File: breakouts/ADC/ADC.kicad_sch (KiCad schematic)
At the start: 5 parts, among them U3 ADS1015IDGS

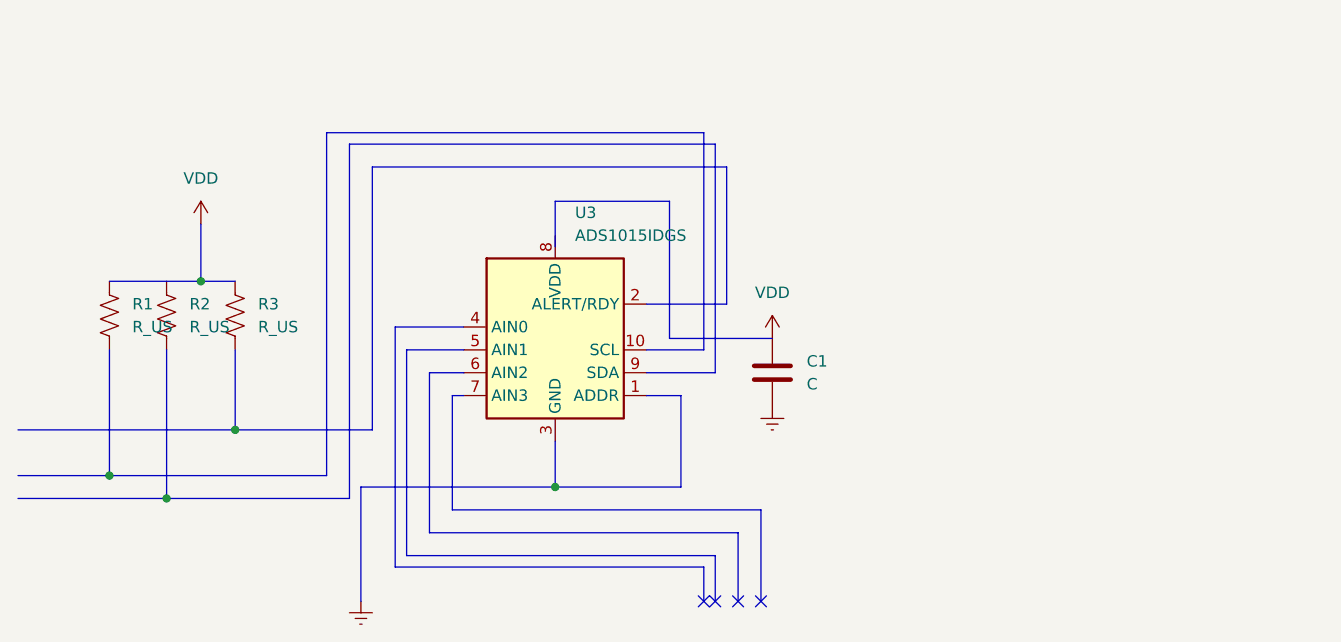
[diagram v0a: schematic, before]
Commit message: Feat[Breakouts}: Bus to wire, organized
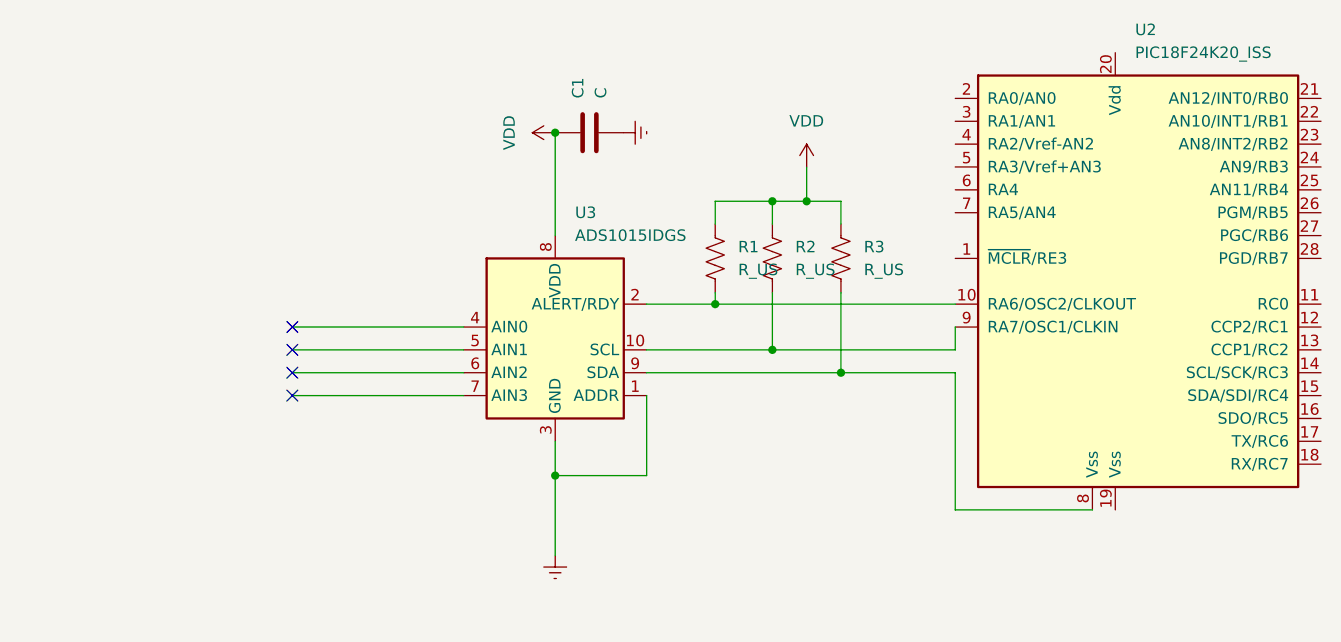
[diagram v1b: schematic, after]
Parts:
- added U2: PIC18F24K20_ISS, Package_SO:SSOP-28_5.3x10.2mm_P0.65mm, symbol MCU_Microchip_PIC18:PIC18F24K20_ISS
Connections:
- net Earth: now also U3.1 (ADDR), U3.3 (GND)
- net VDD: now also R1.1, R2.1, R3.1, U3.8 (VDD)
- net at R1.2: now also U3.2 (ALERT/RDY), U2.10 (RA6/OSC2/CLKOUT)
- net at R3.2: now also U3.9 (SDA), U2.8 (Vss)
- net at R2.2: now also U3.10 (SCL), U2.9 (RA7/OSC1/CLKIN)
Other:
- moved on the sheet: C1, R1, R2, R3

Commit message: Feat[breakouts]: Added TODOs for ADC
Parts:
- added R4: R_Small, symbol Device:R_Small
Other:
- note added: ""earth" ground means that electricity is physically connected to the earth, so that excess surges of electricity can dissipate. In this case we are referring to ground as the common return path for electricity (once your ADC is powered by VDD electricity needs a path to flow back!), so we want to use this symbol."
- note added: "1"
- note added: "1. This is the "earth" ground symbol, which is actually different to the symbol."
- note added: "2"
- note added: "2. Same as 1 - change to the the corrent GND symbol. Also, the GND symbol typically points towards the bottom so u want to rotate this to point to the bottom"
- note added: "3"
- note added: "3. The VDD symbol usually points upwards. You did it for the pull-up resistors so just rotate this upwards"
- note added: "4"
- note added: "4. Rmb this is a breakout board so u don't actually need to slap an MCU on the board. U can just break out the i2c pins (take a look at varit's INA226 breakout board) which can be connected to a pico or arduino or the many other alternatives we alrdy have. But great job thinking above and beyond!"
- note added: "5"
- note added: "5. This is the US symbol for a resistor, we typically use the international resistor symbol. Also, you don't actually need to pull the i2c lines high on a breakout board as it will already be pulled high from the master/central side. So you can remove R2 and R3"
- note added: "6"
- note added: "6. Okay, you've pulled ADDR low, meaning that you will have one i2c address. But what if there are address collisions between peripherals? What if you need to change the address? Read section 8.5 (pages 18-19) of your datasheet and see if you can provide alternative addresses using jumpers (look at varit's INA226 board)"
- note added: "7"
- note added: "7. What's the point of the ADC if it can't take any inputs? You need to break these pins out (probably with a 1x4 2.54mm header pin) so the chip can actually take in an analog input and convert it."
- note added: "Crane, this is some great work you've done. I can see you've put a lot of thought into the schematic and payed a lot of attention to the datasheet. I've left some feedback which you can work on. Also, make sure to reference Byran's ADC in his carrier schematic, and take a look at the other boards in the breakouts folder to get a better sense of what you are doing. Good job!"
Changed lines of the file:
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@@
     (stroke (width 0) (type default))
   )
+  (text "6" (exclude_from_sim no)
+ (at 148.336 93.472 0)
+    (effects (font (size 1.27 1.27)))
+  )
+  (text "1. This is the \"earth\" ground symbol, which is actually different to the     symbol.\n" (exclude_from_sim no)
+    (at 105.156 133.096 0)
+    (effects (font (size 1.27 1.27)))
+  )
+  (text "4. Rmb this is a breakout board so u don't actually need to slap an MCU on the board.\nU can just break out the i2c pins (take a look at varit's INA226 breakout board)\nwhich can be connected to a pico or arduino or the \nmany other alternatives we alrdy have. But great job thinking above and beyond!" (exclude_from_sim no)
+    (at 183.388 113.538 0)
+    (effects (font (size 1.27 1.27)) (justify left))
+  )
+  (text "5. This is the US symbol for a resistor, we typically use the international resistor\nsymbol. Also, you don't actually need to pull the i2c lines high on a breakout board\nas it will already be pulled high from the master/central side. So you can remove R2 and R3" (exclude_from_sim no)
+    (at 174.244 42.926 0)
+    (effects (font (size 1.27 1.27)) (justify left))
+  )
+  (text "7. What's the point of the ADC if it can't take any inputs? You need to break these\npins out (probably with a 1x4 2.54mm header pin) so the chip can actually take in an \nanalog input and convert it." (exclude_from_sim no)
+    (at 16.256 79.502 0)
+    (effects (font (size 1.27 1.27)) (justify left))
+  )
+  (text "2. Same as 1 - change to the the corrent GND symbol. Also, the GND symbol typically points towards\nthe bottom so u want to rotate this to point to the bottom" (exclude_from_sim no)
+    (at 48.514 40.64 0)
+    (effects (font (size 1.27 1.27)) (justify left))
+  )
+  (text "\"earth\" ground means that electricity is physically connected to the\nearth, so that excess surges of electricity can dissipate. In this case we are referring\nto ground as the common return path for electricity (once your ADC is powered by VDD\nelectricity needs a path to flow back!), so we want to use this      symbol." (exclude_from_sim no)
+    (at 62.484 140.208 0)
+    (effects (font (size 1.27 1.27)) (justify left))
+  )
+  (text "5" (exclude_from_sim no)
+ (at 170.688 72.644 0)
+    (effects (font (size 1.27 1.27)))
+  )
+  (text "Crane, this is some great work you've done. I can see you've put a lot of thought\ninto the schematic and payed a lot of attention to the datasheet. I've left some\nfeedback which you can work on. Also, make sure to reference Byran's ADC in his carrier\nschematic, and take a look at the other boards in the breakouts folder to get a better\nsense of what you are doing. Good job!" (exclude_from_sim no)
+    (at 224.536 144.526 0)
+    (effects (font (size 1.27 1.27)))
+  )
+  (text "3" (exclude_from_sim no)
+ (at 134.366 65.278 0)
+    (effects (font (size 1.27 1.27)))
+  )
+  (text "6. Okay, you've pulled ADDR low, meaning that you will have one i2c address. But what if \nthere are address collisions between peripherals? What if you need to change the address?\nRead section 8.5 (pages 18-19) of your datasheet and see if you can provide alternative\naddresses using jumpers (look at varit's INA226 board)" (exclude_from_sim no)
+    (at 19.812 118.872 0)
+    (effects (font (size 1.27 1.27)) (justify left))
+  )
+  (text "2" (exclude_from_sim no)
+ (at 148.59 60.706 0)
+    (effects (font (size 1.27 1.27)))
+  )
+  (text "1" (exclude_from_sim no)
+ (at 134.366 112.522 0)
+    (effects (font (size 1.27 1.27)))
+  )
+  (text "7" (exclude_from_sim no)
+ (at 112.522 88.392 0)
+    (effects (font (size 1.27 1.27)))
+  )
+  (text "4" (exclude_from_sim no)
+ (at 218.694 104.14 0)
+    (effects (font (size 1.27 1.27)))
+  )
+  (text "3. The VDD symbol usually points upwards. You did it for the pull-up resistors so just\nrotate this upwards" (exclude_from_sim no)
+    (at 49.022 46.228 0)
+    (effects (font (size 1.27 1.27)) (justify left))
+  )
   (symbol (lib_id "power:Earth") (at 137.16 109.22 0) (unit 1)
     (exclude_from_sim no) (in_bom yes) (on_board yes) (dnp no) (fields_autoplaced)
@@
     )
   )
+  (symbol (lib_id "power:GND") (at 139.954 130.81 0) (unit 1)
+    (exclude_from_sim no) (in_bom yes) (on_board yes) (dnp no) (fields_autoplaced)
+    (property "Reference" "#PWR05" (at 139.954 137.16 0)
+      (effects (font (size 1.27 1.27)) hide)
+    )
+    (property "Value" "GND" (at 139.954 135.89 0)
+      (effects (font (size 1.27 1.27)))
+    )
+    (property "Footprint" "" (at 139.954 130.81 0)
+      (effects (font (size 1.27 1.27)) hide)
+    )
+    (property "Datasheet" "" (at 139.954 130.81 0)
+      (effects (font (size 1.27 1.27)) hide)
+    )
+    (property "Description" "Power symbol creates a global label with name \"GND\" , ground" (at 139.954 130.81 0)
+      (effects (font (size 1.27 1.27)) hide)
+    )
+    (pin "1")
+    (instances
+      (project "ADC"
+        (path "/20192dbe-2de0-4922-ac80-f57202ca439d"
+          (reference "#PWR05") (unit 1)
+        )
+      )
+    )
+  )
   (symbol (lib_id "power:VDD") (at 165.1 66.04 0) (unit 1)
     (exclude_from_sim no) (in_bom yes) (on_board yes) (dnp no) (fields_autoplaced)
@@
         (path "/20192dbe-2de0-4922-ac80-f57202ca439d"
           (reference "#PWR01") (unit 1)
+        )
+      )
+    )
+  )
+  (symbol (lib_id "Device:R_Small") (at 267.97 40.132 90) (unit 1)
+    (exclude_from_sim no) (in_bom yes) (on_board yes) (dnp no) (fields_autoplaced)
+    (property "Reference" "R4" (at 267.97 34.29 90)
+      (effects (font (size 1.27 1.27)))
+    )
+    (property "Value" "R_Small" (at 267.97 36.83 90)
+      (effects (font (size 1.27 1.27)))
+    )
+    (property "Footprint" "" (at 267.97 40.132 0)
+      (effects (font (size 1.27 1.27)) hide)
+    )
+    (property "Datasheet" "~" (at 267.97 40.132 0)
+      (effects (font (size 1.27 1.27)) hide)
+    )
+    (property "Description" "Resistor, small symbol" (at 267.97 40.132 0)
+      (effects (font (size 1.27 1.27)) hide)
+    )
+    (pin "1")
+    (pin "2")
+    (instances
+      (project "ADC"
+        (path "/20192dbe-2de0-4922-ac80-f57202ca439d"
+          (reference "R4") (unit 1)
         )
       )
@@
         )
       )
+    )
+  )
+  (symbol (lib_id "power:GND") (at 132.842 141.732 0) (unit 1)
+    (exclude_from_sim no) (in_bom yes) (on_board yes) (dnp no) (fields_autoplaced)
+    (property "Reference" "#PWR06" (at 132.842 148.082 0)
+      (effects (font (size 1.27 1.27)) hide)
+    )
+    (property "Value" "GND" (at 132.842 146.812 0)
+      (effects (font (size 1.27 1.27)))
+    )
+    (property "Footprint" "" (at 132.842 141.732 0)
+      (effects (font (size 1.27 1.27)) hide)
+    )
+    (property "Datasheet" "" (at 132.842 141.732 0)
+      (effects (font (size 1.27 1.27)) hide)
+    )
+    (property "Description" "Power symbol creates a global label with name \"GND\" , ground" (at 132.842 141.732 0)
+      (effects (font (size 1.27 1.27)) hide)
+    )
+    (pin "1")
+    (instances
+      (project "ADC"
+        (path "/20192dbe-2de0-4922-ac80-f57202ca439d"
+          (reference "#PWR06") (unit 1)
+        )
+      )

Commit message: Feat[breakouts]: Fixed some ToDOs
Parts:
- removed R1, R2, R3: R_US, symbol Device:R_US
- removed U2: PIC18F24K20_ISS, Package_SO:SSOP-28_5.3x10.2mm_P0.65mm, symbol MCU_Microchip_PIC18:PIC18F24K20_ISS
- added J1: Conn_01x04_Pin, symbol Connector:Conn_01x04_Pin
- added R1: R_Small, symbol Device:R_Small
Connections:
- net Earth is gone; now on net GND: C1.2, U3.1 (ADDR), U3.3 (GND)
- net VDD: now also R1.1
- net at U3.2 (ALERT/RDY): now also U3.10 (SCL), U3.9 (SDA), R1.2
- net at U3.4 (AIN0): now also J1.1 (Pin_1)
- net at U3.5 (AIN1): now also J1.2 (Pin_2)
- net at U3.6 (AIN2): now also J1.3 (Pin_3)
- net at U3.7 (AIN3): now also J1.4 (Pin_4)
- no-connect marks 4 -> 0
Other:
- note added: "I don't really understand step 5. I know that the SDA line transmits data and the SCL gives out clock signals. However, I don't know how to incorporate that into the board. Do I connect it all to one resistor?"
- note removed: "7"
